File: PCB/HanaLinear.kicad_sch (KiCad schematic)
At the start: 67 parts, among them SW1 Esc, SW10 7, SW11 8, SW12 9, SW13 0, SW14 -, SW15 =, SW16 Delete, SW17 F7, SW18 F8, SW19 F9, SW2 `, SW20 Tab, SW21 Q, SW22 W, SW23 E, SW24 R, SW25 T, SW26 Y, SW27 U, SW28 I, SW29 O, SW3 F3, SW30 P, SW31 [, SW32 ], SW33 |, SW34 CapsLock, SW35 Left Shift, SW36 A, SW37 S, SW38 D, SW39 F, SW4 1, SW40 G, SW41 H, SW42 J, SW43 K, SW44 L, SW45 ;, SW46 Return, SW47 Z, SW48 X, SW49 C, SW5 2, SW50 V, SW51 B, SW52 N, SW53 M, SW54 ,, SW55 ., SW56 /, SW57 Right Shift, SW58 ', SW59 Fn, SW6 3, SW60 Control, SW61 Option, SW62 Command, SW63 Left, SW64 Down, SW65 Up, SW66 Right, SW67 Space, SW7 4, SW8 5, SW9 6

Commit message: grr
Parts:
- added D1, D10, D11, D12, D13, D14, D15, D16, D17, D18, D19, D2, D20, D21, D22, D23, D24, D25, D26, D27, D28, D29, D3, D30, D31, D32, D33, D34, D35, D36, D37, D38, D39, D4, D40, D41, D42, D43, D44, D45, D46, D47, D48, D49, D5, D50, D51, D52, D53, D54, D55, D56, D57, D58, D59, D6, D60, D61, D62, D63, D64, D66, D67, D68, D7, D8, D9: D_Small, symbol Device:D_Small
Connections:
- net at SW66.1: now also SW59.1, SW60.1, SW61.1, SW62.1, SW63.1, SW64.1, SW65.1, SW67.1
- net at SW66.2: now also D32.1 (K), D33.2 (A)
- net at SW49.1: now also SW35.1, SW47.1, SW48.1, SW50.1, SW51.1, SW52.1, SW53.1, SW54.1, SW55.1, SW56.1, SW57.1
- net at SW49.2: now also D49.2 (A), D51.1 (K)
- net at SW33.1: now also SW20.1, SW21.1, SW22.1, SW23.1, SW24.1, SW25.1, SW26.1, SW27.1, SW28.1, SW29.1, SW30.1, SW31.1, SW32.1
- net at SW33.2: now also D29.1 (K), D30.2 (A)
- net at SW37.1: now also SW34.1, SW36.1, SW38.1, SW39.1, SW40.1, SW41.1, SW42.1, SW43.1, SW44.1, SW45.1, SW46.1, SW58.1
- net at SW37.2: now also D10.2 (A), D9.1 (K)
- net at SW46.2: now also D30.1 (K), D31.2 (A)
- net at SW27.2: now also D20.1 (K), D21.2 (A)
- net at SW60.2: now also D57.2 (A), D58.1 (K)
- net at SW29.2: now also D62.1 (K), D63.2 (A)
- net at SW65.2: now also D67.1 (K), D68.2 (A)
- net at SW44.2: now also D63.1 (K), D64.2 (A)
- net at SW1.1: now also SW17.1, SW18.1, SW19.1, SW3.1
- net at SW1.2: now also D1.2 (A)
- net at SW50.2: now also D52.1 (K), D53.2 (A)
- net at SW8.1: now also SW10.1, SW11.1, SW12.1, SW13.1, SW14.1, SW15.1, SW16.1, SW2.1, SW4.1, SW5.1, SW6.1, SW7.1, SW9.1
- net at SW8.2: now also D48.2 (A)
- net at SW64.2: now also D42.1 (K), D43.2 (A)
- net at SW22.2: now also D8.1 (K), D9.2 (A)
- net at SW31.2: now also D39.1 (K), D40.2 (A)
- net at SW38.2: now also D45.1 (K), D46.2 (A)
- net at SW17.2: now also D13.2 (A)
- net at SW21.2: now also D59.1 (K), D60.2 (A)
- net at SW32.2: now also D67.2 (A)
- net at SW5.2: now also D59.2 (A)
- net at SW48.2: now also D46.1 (K), D47.2 (A)
- net at SW54.2: now also D64.1 (K), D66.2 (A)
- net at SW10.2: now also D13.1 (K), D14.2 (A)
- net at SW24.2: now also D48.1 (K), D50.2 (A)
- net at SW13.2: now also D62.2 (A)
- net at SW2.2: now also D1.1 (K), D2.2 (A)
- net at SW63.2: now also D37.1 (K), D38.2 (A)
- net at SW42.2: now also D21.1 (K), D22.2 (A)
- net at SW23.2: now also D44.1 (K), D45.2 (A)
- net at SW12.2: now also D24.1 (K), D25.2 (A)
- net at SW14.2: now also D34.2 (A)
- net at SW34.2: now also D3.1 (K), D4.2 (A)
- net at SW30.2: now also D34.1 (K), D35.2 (A)
- net at SW35.2: now also D4.1 (K), D5.2 (A)
- net at SW36.2: now also D60.1 (K), D61.2 (A)
- net at SW7.2: now also D44.2 (A)
- net at SW15.2: now also D39.2 (A)
- net at SW11.2: now also D19.1 (K), D20.2 (A)
- net at SW19.2: now also D24.2 (A)
- net at SW40.2: now also D52.2 (A), D54.1 (K)
- net at SW59.2: now also D5.1 (K), D6.2 (A)
- net at SW62.2: now also D11.1 (K), D12.2 (A)
- net at SW51.2: now also D16.1 (K), D17.2 (A)
- net at SW45.2: now also D35.1 (K), D36.2 (A)
- net at SW41.2: now also D15.1 (K), D16.2 (A)
- net at SW43.2: now also D26.1 (K), D27.2 (A)
- net at SW55.2: now also D36.1 (K), D37.2 (A)
- net at SW18.2: now also D19.2 (A)
- net at SW4.2: now also D58.2 (A)
- net at SW56.2: now also D41.1 (K), D42.2 (A)
- net at SW47.2: now also D10.1 (K), D11.2 (A)
- net at SW67.2: now also D17.1 (K), D18.2 (A)
- net at SW3.2: now also D7.2 (A)
- net at SW20.2: now also D2.1 (K), D3.2 (A)
- net at SW9.2: now also D55.2 (A)
- net at SW57.2: now also D31.1 (K), D32.2 (A)
- net at SW6.2: now also D7.1 (K), D8.2 (A)
- net at SW39.2: now also D50.1 (K), D51.2 (A)
- net at SW53.2: now also D27.1 (K), D28.2 (A)
- net at SW52.2: now also D22.1 (K), D23.2 (A)
- net at SW25.2: now also D54.2 (A), D55.1 (K)
- net at SW58.2: now also D40.1 (K), D41.2 (A)
- net at SW16.2: now also D29.2 (A)
- net at SW61.2: now also D56.2 (A), D61.1 (K)
- net at SW28.2: now also D25.1 (K), D26.2 (A)
- net at SW26.2: now also D14.1 (K), D15.2 (A)

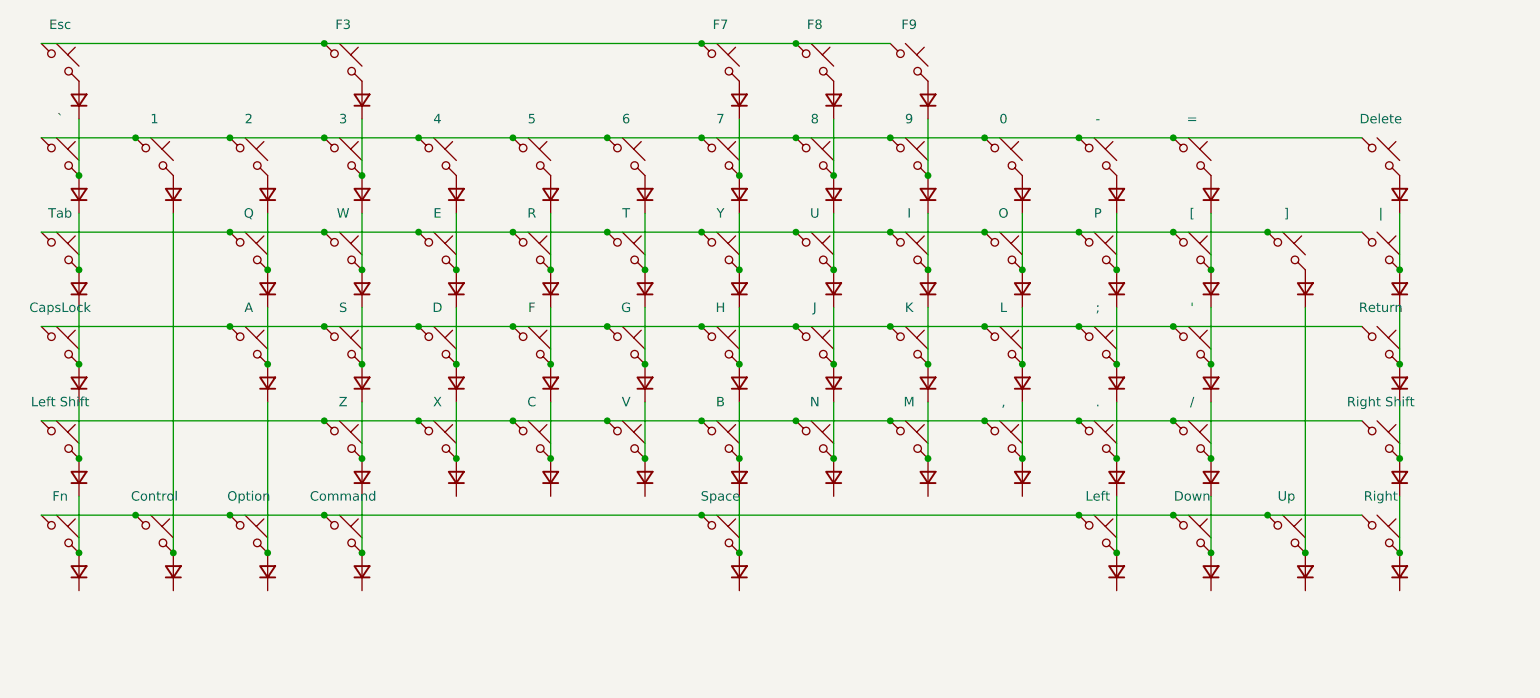
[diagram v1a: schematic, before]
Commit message: add row/col labels
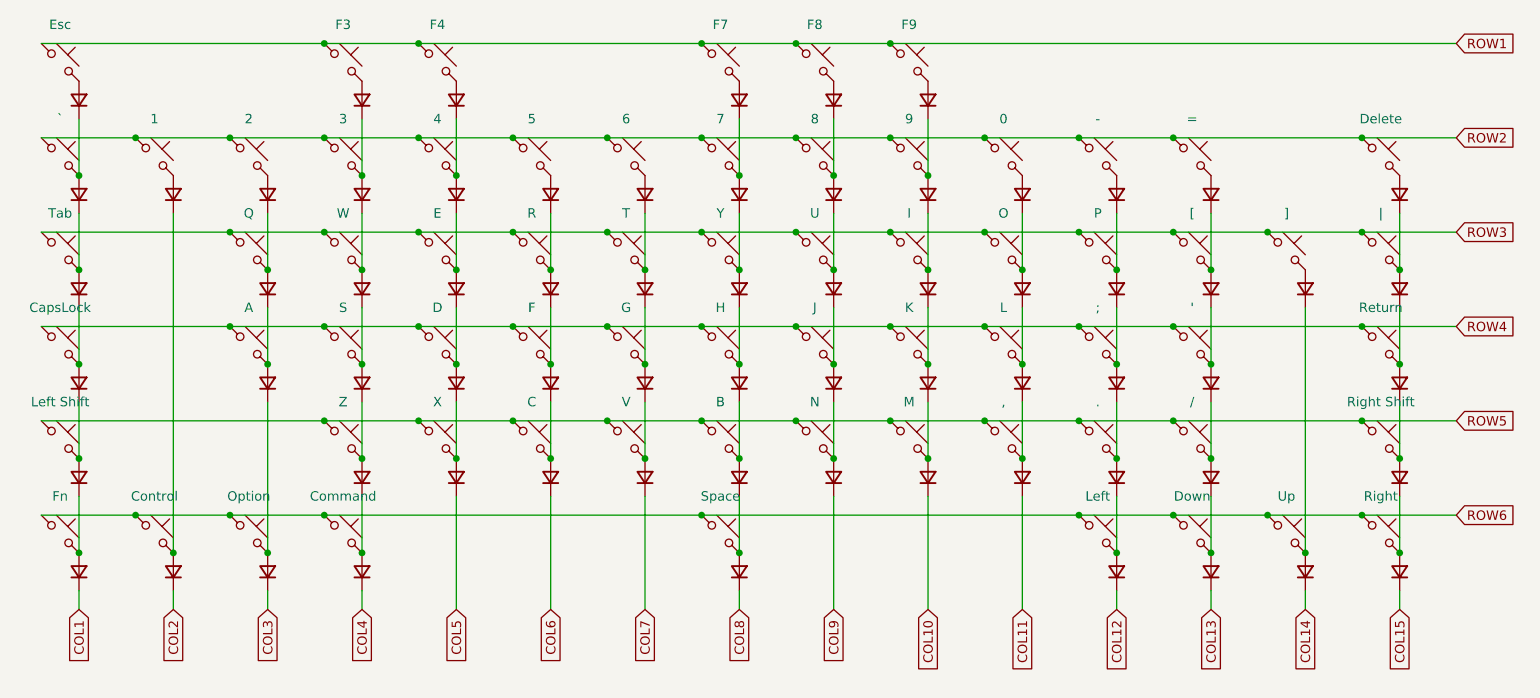
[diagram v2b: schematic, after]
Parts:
- added D65: D_Small, symbol Device:D_Small
- added SW68: F4, symbol Switch:SW_Push_45deg
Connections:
- net ROW6: now reaches SW59.1, SW60.1, SW61.1, SW62.1, SW63.1, SW64.1, SW65.1, SW66.1, SW67.1
- net ROW5: now reaches SW35.1, SW47.1, SW48.1, SW49.1, SW50.1, SW51.1, SW52.1, SW53.1, SW54.1, SW55.1, SW56.1, SW57.1
- net ROW3: now reaches SW20.1, SW21.1, SW22.1, SW23.1, SW24.1, SW25.1, SW26.1, SW27.1, SW28.1, SW29.1, SW30.1, SW31.1, SW32.1, SW33.1
- net ROW4: now reaches SW34.1, SW36.1, SW37.1, SW38.1, SW39.1, SW40.1, SW41.1, SW42.1, SW43.1, SW44.1, SW45.1, SW46.1, SW58.1
- net COL5: now reaches D47.1 (K)
- net COL11: now reaches D66.1 (K)
- net ROW1: now reaches SW1.1, SW17.1, SW18.1, SW19.1, SW3.1
- net ROW1: now also SW68.1
- net COL9: now reaches D23.1 (K)
- net COL12: now reaches D38.1 (K)
- net ROW2: now reaches SW10.1, SW11.1, SW12.1, SW13.1, SW14.1, SW15.1, SW16.1, SW2.1, SW4.1, SW5.1, SW6.1, SW7.1, SW8.1, SW9.1
- net COL13: now reaches D43.1 (K)
- net COL6: now reaches D49.1 (K)
- net COL1: now reaches D6.1 (K)
- net COL15: now reaches D33.1 (K)
- net COL8: now reaches D18.1 (K)
- net at D44.2 (A), SW7.2: now also D65.1 (K)
- net COL10: now reaches D28.1 (K)
- net COL4: now reaches D12.1 (K)
- net COL3: now reaches D56.1 (K)
- net COL14: now reaches D68.1 (K)
- net COL7: now reaches D53.1 (K)
- net COL2: now reaches D57.1 (K)
- new net: D65.2 (A), SW68.2

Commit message: grr
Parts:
- added U1: RP2040, Package_DFN_QFN:QFN-56-1EP_7x7mm_P0.4mm_EP3.2x3.2mm, symbol MCU_RaspberryPi:RP2040
- renumbered D8 to D10, D44 to D11, D48 to D12, D55 to D13, D20 to D15, D25 to D16, D62 to D17, D34 to D18, D39 to D19, D7 to D2, D29 to D20, D3 to D21, D60 to D22, D9 to D23, D45 to D24, D50 to D25, D54 to D26, D15 to D27, D21 to D28, D26 to D29, D65 to D3, D63 to D30, D35 to D31, D40 to D32, D67 to D33, D30 to D34, D4 to D35, D61 to D36, D10 to D37, D46 to D38, D51 to D39, D13 to D4, D52 to D40, D16 to D41, D22 to D42, D27 to D43, D64 to D44, D36 to D45, D41 to D46, D31 to D47, D5 to D48, D11 to D49, D19 to D5, D47 to D50, D49 to D51, D53 to D52, D17 to D53, D23 to D54, D28 to D55, D66 to D56, D37 to D57, D42 to D58, D32 to D59, D24 to D6, D6 to D60, D57 to D61, D56 to D62, D12 to D63, D18 to D64, D38 to D65, D43 to D66, D68 to D67, D33 to D68, D2 to D7, D58 to D8, D59 to D9, SW6 to SW10, SW7 to SW11, SW8 to SW12, SW9 to SW13, SW10 to SW14, SW11 to SW15, SW12 to SW16, SW13 to SW17, SW14 to SW18, SW15 to SW19, SW3 to SW2, SW16 to SW20, SW20 to SW21, SW21 to SW22, SW22 to SW23, SW23 to SW24, SW24 to SW25, SW25 to SW26, SW26 to SW27, SW27 to SW28, SW28 to SW29, SW68 to SW3, SW29 to SW30, SW30 to SW31, SW31 to SW32, SW32 to SW33, SW33 to SW34, SW34 to SW35, SW17 to SW4, SW58 to SW46, SW46 to SW47, SW35 to SW48, SW47 to SW49, SW18 to SW5, SW48 to SW50, SW49 to SW51, SW50 to SW52, SW51 to SW53, SW52 to SW54, SW53 to SW55, SW54 to SW56, SW55 to SW57, SW56 to SW58, SW57 to SW59, SW19 to SW6, SW59 to SW60, SW60 to SW61, SW61 to SW62, SW62 to SW63, SW67 to SW64, SW63 to SW65, SW64 to SW66, SW65 to SW67, SW66 to SW68, SW2 to SW7, SW4 to SW8, SW5 to SW9
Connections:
- new net: U1.1 (IOVDD), U1.10 (IOVDD), U1.22 (IOVDD), U1.33 (IOVDD), U1.42 (IOVDD), U1.49 (IOVDD)
- new net: U1.23 (DVDD), U1.50 (DVDD)

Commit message: OH MY GOD
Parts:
- added C1: 0.001uF, symbol Device:C
- added C10, C11, C12, C13, C14, C15, C16, C17, C6, C7, C9: 100nF, symbol Device:C_Small
- added C18: 100n, symbol Device:C_Small
- added C19, C20: 15pF, symbol Device:C
- added C2: 0.1uF, symbol Device:C
- added C3, C4: 10uF, symbol Device:C
- added C5, C8: 1uF, symbol Device:C_Small
- added H1, H2, H3, H4: MountingHole_Pad, symbol Mechanical:MountingHole_Pad
- added J1: USB_C_Receptacle_USB2.0_14P, symbol Connector:USB_C_Receptacle_USB2.0_14P
- added J2: SW, symbol Connector:Conn_01x02_Pin
- added R1, R2: 5.1K, symbol Device:R_Small
- added R3: 1M, symbol Device:R
- added R4, R5: 1k, symbol Device:R
- added R6, R7: 10K, symbol Device:R
- added R8, R9: 27, symbol Device:R
- added SW69: Brightness, symbol Device:RotaryEncoder
- added SW70: Volume, symbol Device:RotaryEncoder_Switch
- added SW71: USB_BOOT, symbol Switch:SW_Push
- added SW72: BOOTSEL, symbol Switch:SW_Push
- added SW73: RESET, symbol Switch:SW_Push
- added U2: NCP1117-3.3_SOT223, Package_TO_SOT_SMD:SOT-223-3_TabPin2, symbol Regulator_Linear:NCP1117-3.3_SOT223
- added U3: W25Q128JVS, Package_SO:SOIC-8_5.3x5.3mm_P1.27mm, symbol Memory_Flash:W25Q128JVS
- added Y2: ABM8-272-T3, symbol Device:Crystal_GND24
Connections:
- net COL1: now also U1.9 (GPIO7)
- net COL10: now also U1.27 (GPIO16)
- net COL11: now also U1.28 (GPIO17)
- net COL12: now also U1.29 (GPIO18)
- net COL13: now also U1.30 (GPIO19)
- net COL14: now also U1.31 (GPIO20)
- net COL15: now also U1.32 (GPIO21)
- net COL2: now also U1.11 (GPIO8)
- net COL3: now also U1.12 (GPIO9)
- net COL4: now also U1.13 (GPIO10)
- net COL5: now also U1.14 (GPIO11)
- net COL6: now also U1.15 (GPIO12)
- net COL7: now also U1.16 (GPIO13)
- net COL8: now also U1.17 (GPIO14)
- net COL9: now also U1.18 (GPIO15)
- net ROW1: now also U1.3 (GPIO1)
- net ROW2: now also U1.4 (GPIO2)
- net ROW3: now also U1.5 (GPIO3)
- net ROW4: now also U1.6 (GPIO4)
- net ROW5: now also U1.7 (GPIO5)
- net ROW6: now also U1.8 (GPIO6)
- net at U1.1 (IOVDD), U1.10 (IOVDD), U1.22 (IOVDD)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: now also U1.43 (ADC_AVDD), U1.44 (VREG_IN), U1.48 (USB_VDD), C10.2, C11.1, C12.2, C13.1, C14.2, C15.1, C16.2, C17.1, C8.2, C9.1
- net GND: now reaches U1.19 (TESTEN)
- net GND: now also U1.57 (GND), C1.2, C10.1, C11.2, C12.1, C13.2, C14.1, C15.2, C16.1, C17.2, C18.2, C19.2, C2.2, C20.2, C3.2, C4.2, C5.2, C6.2, C7.1, C8.1, C9.2, H1.1, H2.1, H3.1, H4.1, J1.A1 (GND), J1.A12 (GND), J1.B1 (GND), J1.B12 (GND), R1.2, R2.2, R3.2, SW69.C, SW70.C, SW70.S2, SW71.1, SW72.1, SW73.1, U2.1 (GND), U3.4 (GND), Y2.2, Y2.4
- net at U1.2 (GPIO0): now also R6.2, SW72.2
- net at U1.20 (XIN): now also C20.1, Y2.3
- net at U1.21 (XOUT): now also R5.1
- net at U1.23 (DVDD), U1.50 (DVDD): now also U1.45 (VREG_VOUT), C5.1, C6.1, C7.2
- net at U1.24 (SWCLK): now also J2.2 (Pin_2)
- net at U1.25 (SWD): now also J2.1 (Pin_1)
- net at U1.26 (RUN): now also R7.2, SW73.2
- net BrightnessA: now reaches U1.34 (GPIO22)
- net BrightnessA: now also SW69.A
- net BrightnessB: now reaches U1.35 (GPIO23)
- net BrightnessB: now also SW69.B
- net VolumeA: now reaches U1.36 (GPIO24)
- net VolumeA: now also SW70.A
- net VolumeB: now reaches U1.37 (GPIO25)
- net VolumeB: now also SW70.B
- net Mute: now reaches U1.38 (GPIO26_ADC0)
- net Mute: now also SW70.S1
- net at U1.46 (USB_DM): now also R9.1
- net at U1.47 (USB_DP): now also R8.1
- net QSPI_SD3: now reaches U1.51 (QSPI_SD3)
- net QSPI_SD3: now also U3.7 (~{HOLD}/~{RESET}/IO_{3})
- net QSPI_SCLK: now reaches U1.52 (QSPI_SCLK)
- net QSPI_SCLK: now also U3.6 (CLK)
- net QSPI_SD0: now reaches U1.53 (QSPI_SD0)
- net QSPI_SD0: now also U3.5 (DI/IO_{0})
- net QSPI_SD2: now reaches U1.54 (QSPI_SD2)
- net QSPI_SD2: now also U3.3 (~{WP}/IO_{2})
- net QSPI_SD1: now reaches U1.55 (QSPI_SD1)
- net QSPI_SD1: now also U3.2 (DO/IO_{1})
- net QSPI_SS: now reaches U1.56 (QSPI_SS)
- net QSPI_SS: now also R4.2, U3.1 (~{CS})
- new net: R4.1, SW71.2
- new net: J1.A5 (CC1), R1.1
- new net: J1.B5 (CC2), R2.1
- new net: C1.1, C2.1, J1.S1 (SHIELD), R3.1
- new net: C19.1, R5.2, Y2.1
- new net +3V3: C18.1, C4.1, R6.1, R7.1, U2.2 (VO), U3.8 (VCC)
- new net USB_D+: J1.A6 (D+), J1.B6 (D+), R8.2
- new net USB_D-: J1.A7 (D-), J1.B7 (D-), R9.2
- new net VBUS: C3.1, J1.A4 (VBUS), J1.A9 (VBUS), J1.B4 (VBUS), J1.B9 (VBUS), U2.3 (VI)
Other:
- moved on the sheet: U1

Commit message: fah
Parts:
- C1: renamed from C17; footprint (none) -> Capacitor_SMD:C_0201_0603Metric
- C10: footprint (none) -> Capacitor_SMD:C_0201_0603Metric
- C11: renamed from C6; footprint (none) -> Capacitor_SMD:C_0201_0603Metric
- C12: renamed from C8; footprint (none) -> Capacitor_SMD:C_0201_0603Metric
- C13: renamed from C5; footprint (none) -> Capacitor_SMD:C_0201_0603Metric
- C14: renamed from C18; value 100n -> 100nF; footprint (none) -> Capacitor_SMD:C_0201_0603Metric
- C15: renamed from C3; footprint (none) -> Capacitor_SMD:C_0402_1005Metric
- C16: renamed from C4; footprint (none) -> Capacitor_SMD:C_0402_1005Metric
- C17: renamed from C20; footprint (none) -> Capacitor_SMD:C_0201_0603Metric
- C18: renamed from C1; footprint (none) -> Capacitor_SMD:C_0201_0603Metric
- C19: renamed from C2; footprint (none) -> Capacitor_SMD:C_0201_0603Metric
- C2: renamed from C15; footprint (none) -> Capacitor_SMD:C_0201_0603Metric
- C20: renamed from C19; footprint (none) -> Capacitor_SMD:C_0201_0603Metric
- C3: renamed from C16; footprint (none) -> Capacitor_SMD:C_0201_0603Metric
- C4: renamed from C13; footprint (none) -> Capacitor_SMD:C_0201_0603Metric
- C5: renamed from C14; footprint (none) -> Capacitor_SMD:C_0201_0603Metric
- C6: renamed from C11; footprint (none) -> Capacitor_SMD:C_0201_0603Metric
- C7: renamed from C12; footprint (none) -> Capacitor_SMD:C_0201_0603Metric
- C8: renamed from C9; footprint (none) -> Capacitor_SMD:C_0201_0603Metric
- C9: renamed from C7; footprint (none) -> Capacitor_SMD:C_0201_0603Metric
- D1, D10, D11, D12, D13, D14, D15, D16, D17, D18, D19, D2, D20, D21, D22, D23, D24, D25, D26, D27, D28, D29, D3, D30, D31, D32, D33, D34, D35, D36, D37, D38, D39, D4, D40, D41, D42, D43, D44, D45, D46, D47, D48, D49, D5, D50, D51, D52, D53, D54, D55, D56, D57, D58, D59, D6, D60, D61, D62, D63, D64, D65, D66, D67, D68, D7, D8, D9: footprint (none) -> Diode_SMD:D_SOD-323
- H1, H2, H3, H4: footprint (none) -> MountingHole:MountingHole_2.5mm_Pad_Via
- J1: footprint (none) -> Connector_USB:USB_C_Receptacle_Amphenol_12401610E4-2A
- J2: footprint (none) -> Connector_PinSocket_1.00mm:PinSocket_1x02_P1.00mm_Vertical
- R1: renamed from R6; footprint (none) -> Resistor_SMD:R_0201_0603Metric
- R2: renamed from R7; footprint (none) -> Resistor_SMD:R_0201_0603Metric
- R3: renamed from R8; footprint (none) -> Resistor_SMD:R_0201_0603Metric
- R4: renamed from R9; footprint (none) -> Resistor_SMD:R_0201_0603Metric
- R5: renamed from R1; footprint (none) -> Resistor_SMD:R_0201_0603Metric
- R6: renamed from R4; footprint (none) -> Resistor_SMD:R_0201_0603Metric
- R7: renamed from R2; footprint (none) -> Resistor_SMD:R_0201_0603Metric
- R8: renamed from R3; footprint (none) -> Resistor_SMD:R_0201_0603Metric
- R9: renamed from R5; footprint (none) -> Resistor_SMD:R_0201_0603Metric
- SW1, SW20: footprint (none) -> Button_Switch_Keyboard:SW_Cherry_MX_2.00u_PCB
- SW10, SW11, SW12, SW13, SW14, SW15, SW16, SW17, SW18, SW19, SW2, SW3, SW4, SW5, SW6, SW7, SW8, SW9: footprint (none) -> Button_Switch_Keyboard:SW_Cherry_MX_1.00u_PCB
- SW21: renamed from SW69; footprint (none) -> Rotary_Encoder:RotaryEncoder_Bourns_Vertical_PEC12R-3x17F-Sxxxx
- SW22: renamed from SW70; footprint (none) -> Rotary_Encoder:RotaryEncoder_Bourns_Vertical_PEC12R-3x17F-Sxxxx
- SW23: renamed from SW21; footprint (none) -> Button_Switch_Keyboard:SW_Cherry_MX_2.00u_PCB
- SW24: renamed from SW22; footprint (none) -> Button_Switch_Keyboard:SW_Cherry_MX_1.00u_PCB
- SW25: renamed from SW23; footprint (none) -> Button_Switch_Keyboard:SW_Cherry_MX_1.00u_PCB
- SW26: renamed from SW24; footprint (none) -> Button_Switch_Keyboard:SW_Cherry_MX_1.00u_PCB
- SW27: renamed from SW25; footprint (none) -> Button_Switch_Keyboard:SW_Cherry_MX_1.00u_PCB
- SW28: renamed from SW26; footprint (none) -> Button_Switch_Keyboard:SW_Cherry_MX_1.00u_PCB
- SW29: renamed from SW27; footprint (none) -> Button_Switch_Keyboard:SW_Cherry_MX_1.00u_PCB
- SW30: renamed from SW28; footprint (none) -> Button_Switch_Keyboard:SW_Cherry_MX_1.00u_PCB
- SW31: renamed from SW29; footprint (none) -> Button_Switch_Keyboard:SW_Cherry_MX_1.00u_PCB
- SW32: renamed from SW30; footprint (none) -> Button_Switch_Keyboard:SW_Cherry_MX_1.00u_PCB
- SW33: renamed from SW31; footprint (none) -> Button_Switch_Keyboard:SW_Cherry_MX_1.00u_PCB
- SW34: renamed from SW32; footprint (none) -> Button_Switch_Keyboard:SW_Cherry_MX_1.00u_PCB
- SW35: renamed from SW33; footprint (none) -> Button_Switch_Keyboard:SW_Cherry_MX_1.00u_PCB
- SW36: renamed from SW34; footprint (none) -> Button_Switch_Keyboard:SW_Cherry_MX_1.00u_PCB
- SW37: renamed from SW35; footprint (none) -> Button_Switch_Keyboard:SW_Cherry_MX_2.00u_PCB
- SW38: renamed from SW36; footprint (none) -> Button_Switch_Keyboard:SW_Cherry_MX_1.00u_PCB
- SW39: renamed from SW37; footprint (none) -> Button_Switch_Keyboard:SW_Cherry_MX_1.00u_PCB
- SW40: renamed from SW38; footprint (none) -> Button_Switch_Keyboard:SW_Cherry_MX_1.00u_PCB
- SW41: renamed from SW39; footprint (none) -> Button_Switch_Keyboard:SW_Cherry_MX_1.00u_PCB
- SW42: renamed from SW40; footprint (none) -> Button_Switch_Keyboard:SW_Cherry_MX_1.00u_PCB
- SW43: renamed from SW41; footprint (none) -> Button_Switch_Keyboard:SW_Cherry_MX_1.00u_PCB
- SW44: renamed from SW42; footprint (none) -> Button_Switch_Keyboard:SW_Cherry_MX_1.00u_PCB
- SW45: renamed from SW43; footprint (none) -> Button_Switch_Keyboard:SW_Cherry_MX_1.00u_PCB
- SW46: renamed from SW44; footprint (none) -> Button_Switch_Keyboard:SW_Cherry_MX_1.00u_PCB
- SW47: renamed from SW45; footprint (none) -> Button_Switch_Keyboard:SW_Cherry_MX_1.00u_PCB
- SW48: renamed from SW46; footprint (none) -> Button_Switch_Keyboard:SW_Cherry_MX_1.00u_PCB
- SW49: renamed from SW47; footprint (none) -> Button_Switch_Keyboard:SW_Cherry_MX_2.00u_PCB
- SW50: renamed from SW48; footprint (none) -> Button_Switch_Keyboard:SW_Cherry_MX_1.00u_PCB
- SW51: renamed from SW49; footprint (none) -> Button_Switch_Keyboard:SW_Cherry_MX_1.00u_PCB
- SW52: renamed from SW50; footprint (none) -> Button_Switch_Keyboard:SW_Cherry_MX_1.00u_PCB
- SW53: renamed from SW51; footprint (none) -> Button_Switch_Keyboard:SW_Cherry_MX_1.00u_PCB
- SW54: renamed from SW52; footprint (none) -> Button_Switch_Keyboard:SW_Cherry_MX_1.00u_PCB
- SW55: renamed from SW53; footprint (none) -> Button_Switch_Keyboard:SW_Cherry_MX_1.00u_PCB
- SW56: renamed from SW54; footprint (none) -> Button_Switch_Keyboard:SW_Cherry_MX_1.00u_PCB
- SW57: renamed from SW55; footprint (none) -> Button_Switch_Keyboard:SW_Cherry_MX_1.00u_PCB
- SW58: renamed from SW56; footprint (none) -> Button_Switch_Keyboard:SW_Cherry_MX_1.00u_PCB
- SW59: renamed from SW57; footprint (none) -> Button_Switch_Keyboard:SW_Cherry_MX_1.00u_PCB
- SW60: renamed from SW58; footprint (none) -> Button_Switch_Keyboard:SW_Cherry_MX_1.00u_PCB
- SW61: renamed from SW59; footprint (none) -> Button_Switch_Keyboard:SW_Cherry_MX_2.00u_PCB
- SW62: renamed from SW60; footprint (none) -> Button_Switch_Keyboard:SW_Cherry_MX_1.00u_PCB
- SW63: renamed from SW61; footprint (none) -> Button_Switch_Keyboard:SW_Cherry_MX_1.00u_PCB
- SW64: renamed from SW62; footprint (none) -> Button_Switch_Keyboard:SW_Cherry_MX_1.00u_PCB
- SW65: renamed from SW63; footprint (none) -> Button_Switch_Keyboard:SW_Cherry_MX_1.00u_PCB
- SW66: renamed from SW64; footprint (none) -> Button_Switch_Keyboard:SW_Cherry_MX_1.00u_PCB
- SW67: renamed from SW65; footprint (none) -> Button_Switch_Keyboard:SW_Cherry_MX_1.00u_PCB
- SW68: renamed from SW66; footprint (none) -> Button_Switch_Keyboard:SW_Cherry_MX_1.00u_PCB
- SW69: renamed from SW67; footprint (none) -> Button_Switch_Keyboard:SW_Cherry_MX_1.00u_PCB
- SW70: renamed from SW68; footprint (none) -> Button_Switch_Keyboard:SW_Cherry_MX_1.00u_PCB
- SW71: renamed from SW72; footprint (none) -> Button_Switch_THT:SW_PUSH_6mm
- SW72: renamed from SW73; footprint (none) -> Button_Switch_THT:SW_PUSH_6mm
- SW73: renamed from SW71; footprint (none) -> Button_Switch_THT:SW_PUSH_6mm
- Y1: renamed from Y2; footprint (none) -> Crystal:Crystal_SMD_3225-4Pin_3.2x2.5mm
- renumbered U2 to U1, U3 to U2, U1 to U3
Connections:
- net at D61.2 (A), SW63.2: now also D48.1 (K); no longer D8.1 (K)
- net at D60.2 (A), SW62.2: now also D35.1 (K); no longer D48.1 (K)
- net at D48.2 (A), SW50.2: now also D8.1 (K); no longer D35.1 (K)

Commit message: :3c
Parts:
- removed C18: 0.001uF, Capacitor_SMD:C_0201_0603Metric, symbol Device:C
- removed C19: 0.1uF, Capacitor_SMD:C_0201_0603Metric, symbol Device:C
- removed R8: 1M, Resistor_SMD:R_0201_0603Metric, symbol Device:R
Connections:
- net +3V3: now also C1.1, C10.2, C12.2, C2.1, C3.2, C4.1, C5.2, C6.1, C7.2, C8.1, U3.1 (IOVDD), U3.10 (IOVDD), U3.22 (IOVDD), U3.33 (IOVDD), U3.42 (IOVDD), U3.43 (ADC_AVDD), U3.44 (VREG_IN), U3.48 (USB_VDD), U3.49 (IOVDD)
- net GND: now also J1.S1 (SHIELD)
- net +1V1: now reaches C11.1, C13.1, C9.2, U3.23 (DVDD), U3.45 (VREG_VOUT), U3.50 (DVDD)

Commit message: update footprint
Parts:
- J1: footprint Connector_USB:USB_C_Receptacle_Amphenol_12401610E4-2A -> Connector_USB:USB_C_Receptacle_G-Switch_GT-USB-7010ASV
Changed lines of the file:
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@@
 			)
 		)
-		(property "Footprint" "Connector_USB:USB_C_Receptacle_Amphenol_12401610E4-2A"
+		(property "Footprint" "Connector_USB:USB_C_Receptacle_G-Switch_GT-USB-7010ASV"
 			(at 52.07 170.18 0)
 			(effects

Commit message: dskjalfjlkf
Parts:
- removed R1: 10K, Resistor_SMD:R_0201_0603Metric, symbol Device:R
- removed SW71: BOOTSEL, Button_Switch_THT:SW_PUSH_6mm, symbol Switch:SW_Push
- removed U1: NCP1117-3.3_SOT223, Package_TO_SOT_SMD:SOT-223-3_TabPin2, symbol Regulator_Linear:NCP1117-3.3_SOT223
- added U1: AMS1117-3.3, Package_TO_SOT_SMD:SOT-223-3_TabPin2, symbol Regulator_Linear:AMS1117-3.3
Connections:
- net +3V3: now also U1.2 (VO)
- net GND: now also U1.1 (GND)
- net VBUS: now also U1.3 (VI)
- no-connect marks 0 -> 1
